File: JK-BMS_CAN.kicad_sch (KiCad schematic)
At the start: 33 parts, among them J1 BMS1, J2 BMS2, U1 LMR36510ADDA, U2 ADuM1201AR, U3 ADuM1201AR, U4 AP7384-33SA

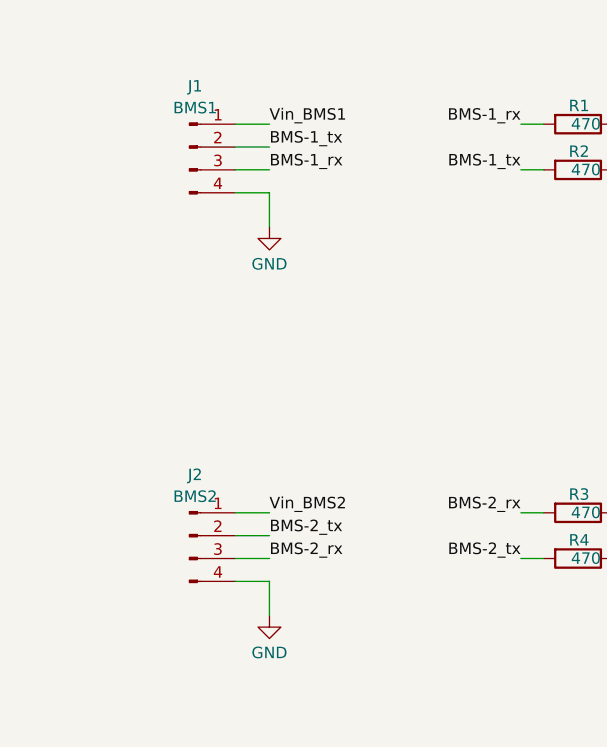
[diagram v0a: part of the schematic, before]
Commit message: changed to rev 1.1
added DTR line for easy flashing
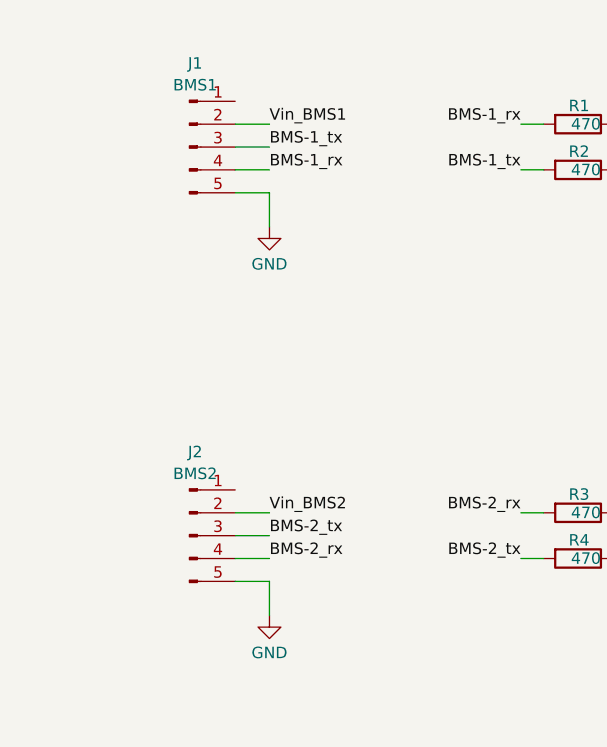
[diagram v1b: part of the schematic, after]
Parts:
- J1, J2: symbol Connector:Conn_01x04_Pin -> Connector:Conn_01x05_Pin
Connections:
- net BMS-1_rx: now also J1.4 (Pin_4); no longer J1.3 (Pin_3)
- net BMS-1_tx: now also J1.3 (Pin_3); no longer J1.2 (Pin_2)
- net BMS-2_rx: now also J2.4 (Pin_4); no longer J2.3 (Pin_3)
- net BMS-2_tx: now also J2.3 (Pin_3); no longer J2.2 (Pin_2)
- net GND: now also J1.5 (Pin_5), J2.5 (Pin_5); no longer J1.4 (Pin_4), J2.4 (Pin_4)
- net Vin_BMS1: now also J1.2 (Pin_2); no longer J1.1 (Pin_1)
- net Vin_BMS2: now also J2.2 (Pin_2); no longer J2.1 (Pin_1)
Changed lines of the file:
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@@
 	)
 	(symbol
-		(lib_id "Connector:Conn_01x04_Pin")
+		(lib_id "Connector:Conn_01x05_Pin")
 		(at 36.83 38.1 0)
 		(unit 1)
@@
 		(fields_autoplaced yes)
 		(property "Reference" "J1"
-			(at 37.465 31.3393 0)
+			(at 37.465 28.7993 0)
 			(effects
 				(font
@@
 		)
 		(property "Value" "BMS1"
-			(at 37.465 33.7636 0)
+			(at 37.465 31.2236 0)
 			(effects
 				(font
@@
 			)
 		)
-		(property "Description" "Generic connector, single row, 01x04, script generated"
+		(property "Description" "Generic connector, single row, 01x05, script generated"
 			(at 36.83 38.1 0)
 			(effects
@@
 		(pin "4"
 		)
+		(pin "5"
+		)
 		(instances
 			(project "JK-BMS_CAN"
@@
 	)
 	(symbol
-		(lib_id "Connector:Conn_01x04_Pin")
+		(lib_id "Connector:Conn_01x05_Pin")
 		(at 36.83 81.28 0)
 		(unit 1)
@@
 		(fields_autoplaced yes)
 		(property "Reference" "J2"
-			(at 37.465 74.5193 0)
+			(at 37.465 71.9793 0)
 			(effects
 				(font
@@
 		)
 		(property "Value" "BMS2"
-			(at 37.465 76.9436 0)
+			(at 37.465 74.4036 0)
 			(effects
 				(font
@@
 			)
 		)
-		(property "Description" "Generic connector, single row, 01x04, script generated"
+		(property "Description" "Generic connector, single row, 01x05, script generated"
 			(at 36.83 81.28 0)
 			(effects
@@
 		(pin "4"
 		)
-		(instances
+		(pin "5"
+		)
+		(instances
